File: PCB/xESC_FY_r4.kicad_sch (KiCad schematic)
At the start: 22 parts, among them J1 Conn_01x09_Male, J10 OM-MB W => MC BRK, J11 Conn_01x04_Pin, J3 Conn_01x05_Male, J4 Conn_01x05_Male, J6 OM-MB U => MC SA, J7 Conn_01x06_Male, J8 Conn_01x06_Pin, J9 OM-MB V => MC +24V, U1 STM32C011F6Px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

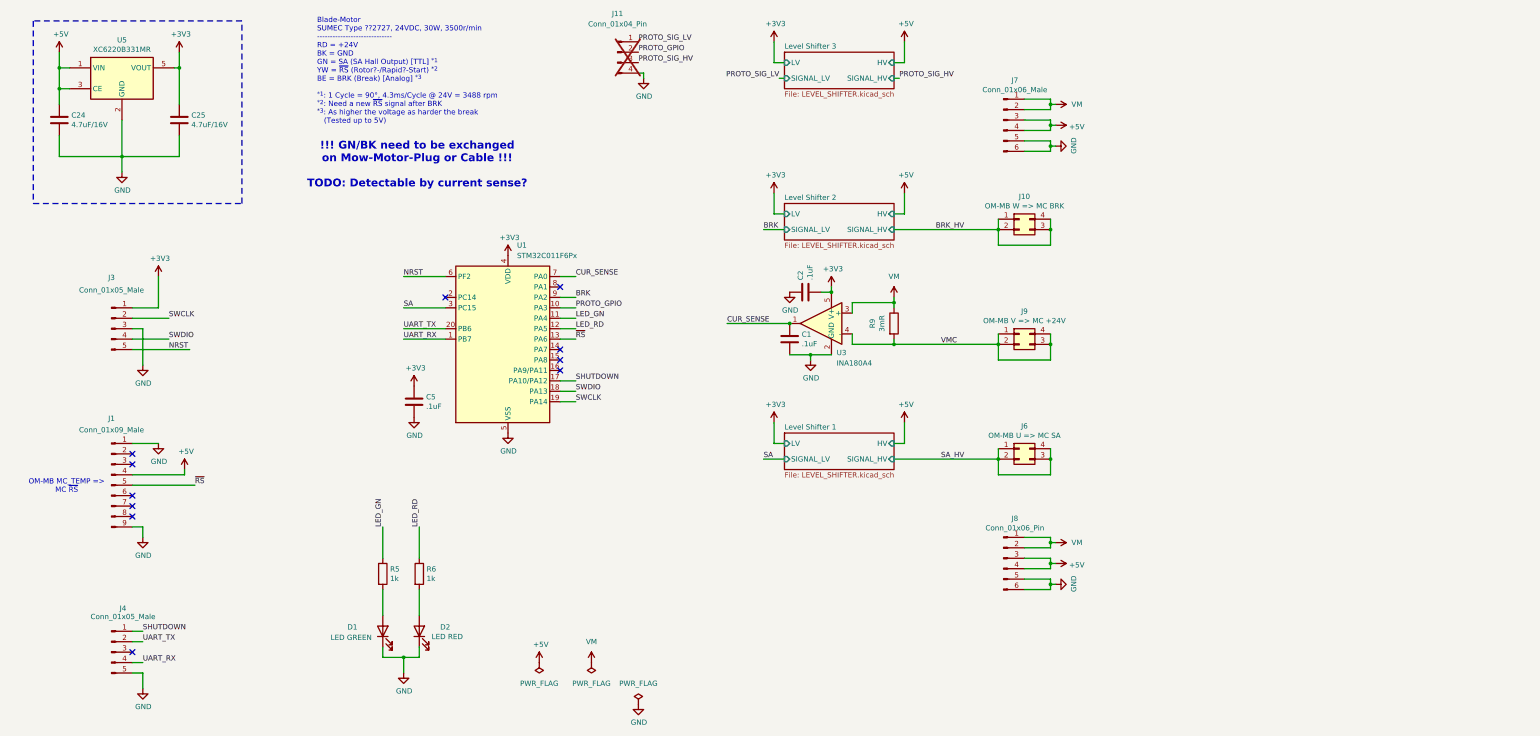
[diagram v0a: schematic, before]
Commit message: Change current sense parts and add SA protection
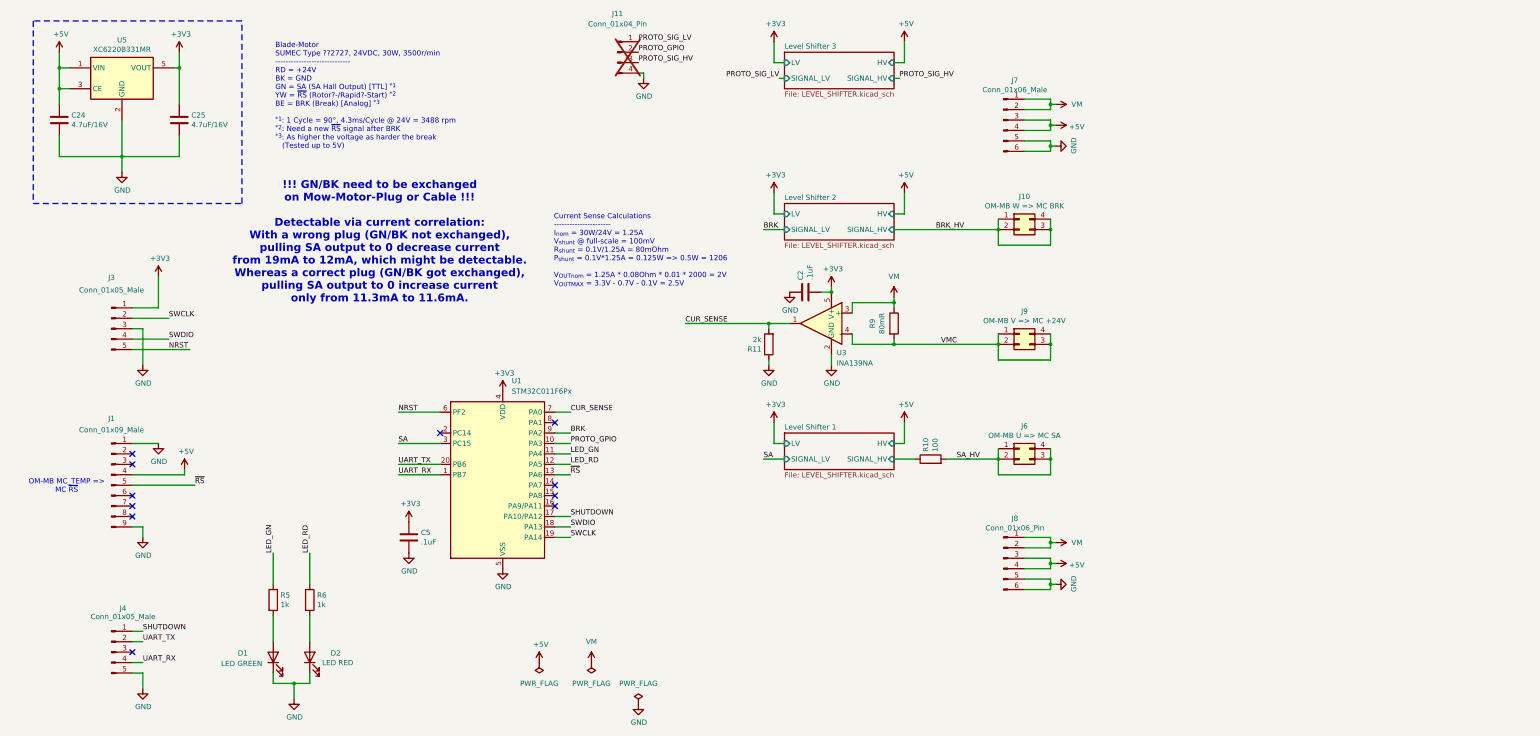
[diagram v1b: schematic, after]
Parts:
- removed C1: .1uF, Capacitor_SMD:C_0603_1608Metric, symbol Device:C
- added R10: 100, Resistor_SMD:R_0603_1608Metric, symbol Device:R
- added R11: 2k, Resistor_SMD:R_0603_1608Metric, symbol Device:R
- R9: value 3mR -> 80mR; footprint Resistor_SMD:R_2512_6332Metric -> Resistor_SMD:R_1206_3216Metric_Pad1.30x1.75mm_HandSolder; Digikey 1712-TLRP3A30DR003FTDGCT-ND -> (none); LCSC C2889862 -> (none); Part Number ARD2512GJR003 -> (none); Stock_PN R-2512-.003-3W-5% -> R-1206-.080-0.5W-1%
- U3: value INA180A4 -> INA139NA; symbol Amplifier_Current:INA180A4 -> Amplifier_Current:INA139
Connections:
- net CUR_SENSE: now also R11.2
- net GND: now also R11.1
- net SA_HV: now also R10.2
- new net Level Shifter 1/SIGNAL_HV: R10.1
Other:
- note added: "!!! GN/BK need to be exchanged on Mow-Motor-Plug or Cable !!! Detectable via current correlation: With a wrong plug (GN/BK not exchanged), pulling SA output to 0 decrease current from 19mA to 12mA, which might be detectable. Whereas a correct plug (GN/BK got exchanged), pulling SA output to 0 increase current only from 11.3mA to 11.6mA."
- note added: "Current Sense Calculations ---------------------- I_{nom} = 30W/24V = 1.25A V_{shunt} @ full-scale = 100mV R_{shunt} = 0.1V/1.25A = 80mOhm P_{shunt} = 0.1V*1.25A = 0.125W => 0.5W = 1206 V_{OUTnom} = 1.25A * 0.08Ohm * 0.01 * 2000 = 2V V_{OUTMAX} = 3.3V - 0.7V - 0.1V = 2.5V"
- note removed: "!!! GN/BK need to be exchanged on Mow-Motor-Plug or Cable !!! TODO: Detectable by current sense?"
- moved on the sheet: C5, D1, D2, R5, R6, U1

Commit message: Bootloader capable UART, high-side power switch, free-wheeling safety, current sense adjustment
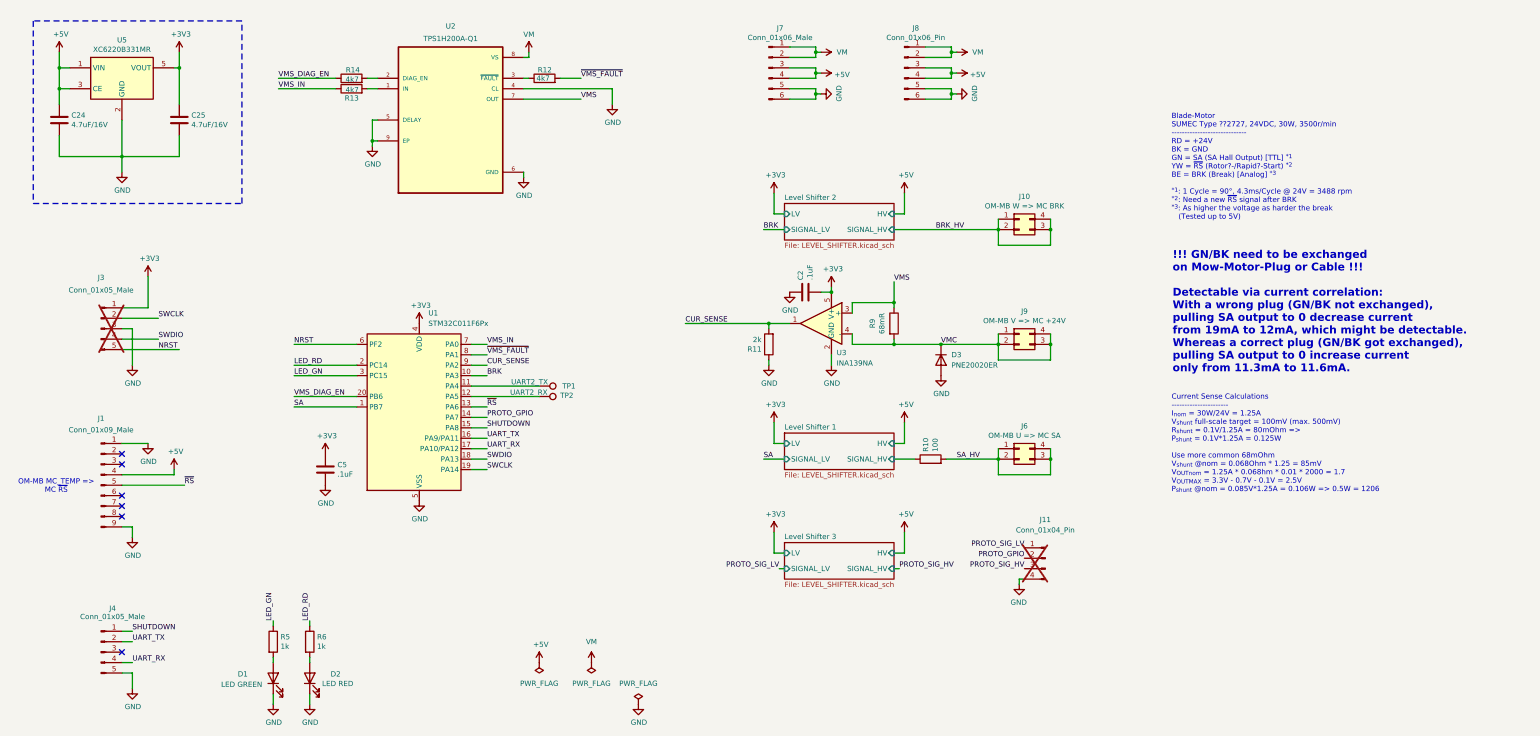
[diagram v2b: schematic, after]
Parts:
- added D3: PNE20020ER, Diode_SMD:Nexperia_CFP3_SOD-123W, symbol Device:D
- added R12, R13, R14: 4k7, Resistor_SMD:R_0603_1608Metric, symbol Device:R
- added TP1: UART2_TX, TestPoint:TestPoint_Pad_1.5x1.5mm, symbol Connector:TestPoint
- added TP2: UART2_RX, TestPoint:TestPoint_Pad_1.5x1.5mm, symbol Connector:TestPoint
- added U2: TPS1H200A-Q1, TPS1H200AQDGNRQ1:SOP65P490X110-9N-AHMOD, symbol TPS1H200AQDGNRQ1:TPS1H200AQDGNRQ1
- J11: now left out of the parts list
- J3: now not fitted; now left out of the parts list
- R9: value 80mR -> 68mR; JLCPCB (none) -> C2442650; Part Number (none) -> KDV12FR068ET
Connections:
- net BRK: now also U1.10 (PA3); no longer U1.9 (PA2)
- net CUR_SENSE: now also U1.9 (PA2); no longer U1.7 (PA0)
- net GND: now also D3.2 (A), U2.4 (CL), U2.5 (DELAY), U2.6 (GND), U2.9 (EP)
- net LED_GN: now also U1.3 (PC15); no longer U1.11 (PA4)
- net LED_RD: now also U1.2 (PC14); no longer U1.12 (PA5)
- net PROTO_GPIO: now also U1.14 (PA7); no longer U1.10 (PA3)
- net SA: now also U1.1 (PB7); no longer U1.3 (PC15)
- net SHUTDOWN: now also U1.15 (PA8); no longer U1.17 (PA10/PA12)
- net UART_RX: now also U1.17 (PA10/PA12); no longer U1.1 (PB7)
- net UART_TX: now also U1.16 (PA9/PA11); no longer U1.20 (PB6)
- net VM: now also U2.8 (VS); no longer R9.1, U3.3 (+)
- net VMC: now also D3.1 (K)
- net ~{VMS_FAULT}: now reaches U1.8 (PA1)
- net ~{VMS_FAULT}: now also R12.2
- new net: R12.1, U2.3 (~{FAULT})
- new net: TP2.1, U1.12 (PA5)
- new net: R13.2, U2.1 (IN)
- new net: R14.2, U2.2 (DIAG_EN)
- new net: TP1.1, U1.11 (PA4)
- new net VMS: R9.1, U2.7 (OUT), U3.3 (+)
- new net VMS_DIAG_EN: R14.1, U1.20 (PB6)
- new net VMS_IN: R13.1, U1.7 (PA0)
- no-connect marks 11 -> 6
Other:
- note added: "Current Sense Calculations ---------------------- I_{nom} = 30W/24V = 1.25A V_{shunt} full-scale target = 100mV (max. 500mV) R_{shunt} = 0.1V/1.25A = 80mOhm => P_{shunt} = 0.1V*1.25A = 0.125W Use more common 68mOhm V_{shunt} @nom = 0.068Ohm * 1.25 = 85mV V_{OUTnom} = 1.25A * 0.068hm * 0.01 * 2000 = 1.7 V_{OUTMAX} = 3.3V - 0.7V - 0.1V = 2.5V P_{shunt} @nom = 0.085V*1.25A = 0.106W => 0.5W = 1206"
- note removed: "Current Sense Calculations ---------------------- I_{nom} = 30W/24V = 1.25A V_{shunt} @ full-scale = 100mV R_{shunt} = 0.1V/1.25A = 80mOhm P_{shunt} = 0.1V*1.25A = 0.125W => 0.5W = 1206 V_{OUTnom} = 1.25A * 0.08Ohm * 0.01 * 2000 = 2V V_{OUTMAX} = 3.3V - 0.7V - 0.1V = 2.5V"
- moved on the sheet: C5, D1, D2, J1, J11, J4, J7, J8, R5, R6, U1
